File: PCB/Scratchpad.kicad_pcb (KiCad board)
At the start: 2 copper layers, 242.9 x 76.2 mm, 52 parts, among them J1 USB_C_Receptacle_USB2.0, J2 I2C, J3 MIDI IN, J4 MIDI OUT, J5 OLED, SW1 Rotary_Encoder_Switch, SW10 SW_SPST, SW11 SW_SPST, SW12 SW_SPST, SW13 SW_SPST, SW14 SW_SPST, SW15 SW_SPST, SW16 SW_SPST, SW17 SW_SPST, SW18 SW_SPST, SW19 SW_SPST, SW2 Rotary_Encoder_Switch, SW20 SW_SPST, SW21 SW_SPST, SW22 SW_SPST, SW23 SW_SPST, SW24 SW_SPST, SW25 SW_SPST, SW26 Rotary_Encoder_Switch, SW3 Rotary_Encoder_Switch, SW4 Rotary_Encoder_Switch, SW5 SW_SPST, SW6 SW_SPST, SW7 SW_SPST, SW8 SW_SPST, SW9 SW_SPST, U1 COM-09032, U2 COM-09032, U3 RP2040TR7, U4 MAX11143ATIT

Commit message: Added some components, I2C is pin header now
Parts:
- J2: footprint Keebio-Parts:TRRS_Jack -> Connector_PinHeader_2.54mm:PinHeader_1x04_P2.54mm_Vertical
- moved U4 41.6 mm to (184.2, 48.4)
- moved J2 4.29 mm to (197.2, 22.8), turned to 0 degrees

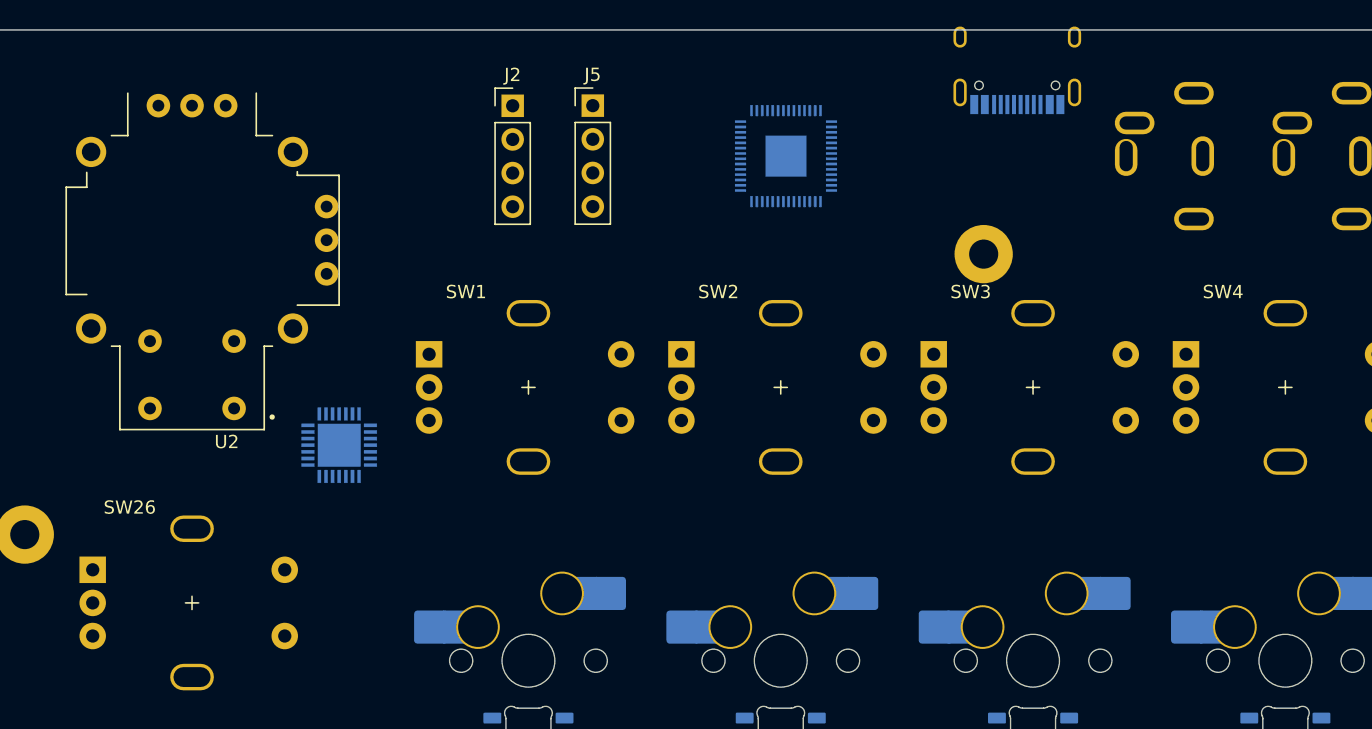
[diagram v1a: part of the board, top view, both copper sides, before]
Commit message: Some footprint updates
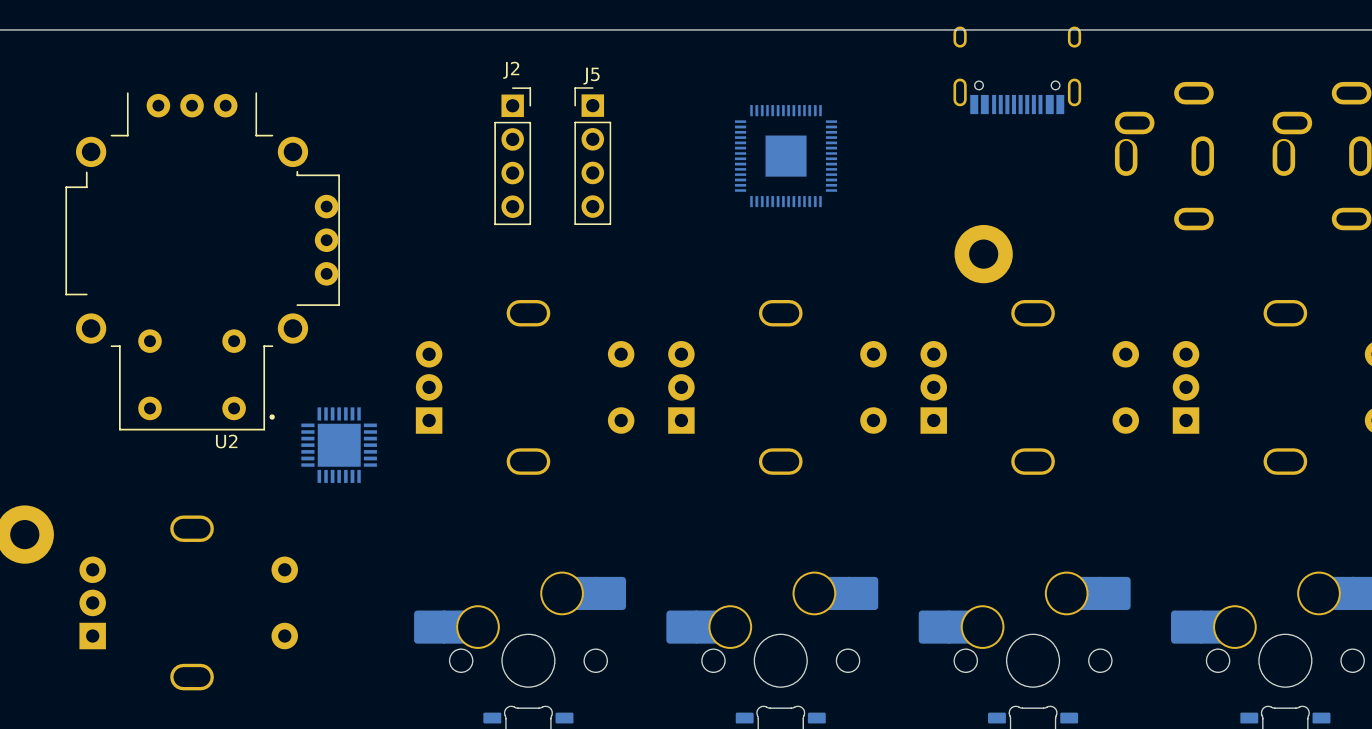
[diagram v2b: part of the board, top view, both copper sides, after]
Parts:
- J2: footprint Connector_PinHeader_2.54mm:PinHeader_1x04_P2.54mm_Vertical -> Connector_PinSocket_2.54mm:PinSocket_1x04_P2.54mm_Vertical
- RV1, RV2, RV3, RV4, RV5, RV6, RV7, RV8: footprint Potentiometer_THT:Potentiometer_Bourns_PTA2043_Single_Slide -> Keebio-Parts:Potentiometer_Bourns_PTA2043_Single_Slide_2
- SW1, SW2, SW26, SW3, SW4: moved to B.Cu
